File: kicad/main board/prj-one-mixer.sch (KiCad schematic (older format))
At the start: 51 parts, among them U301 TL072, U302 TL072, U303 TL072

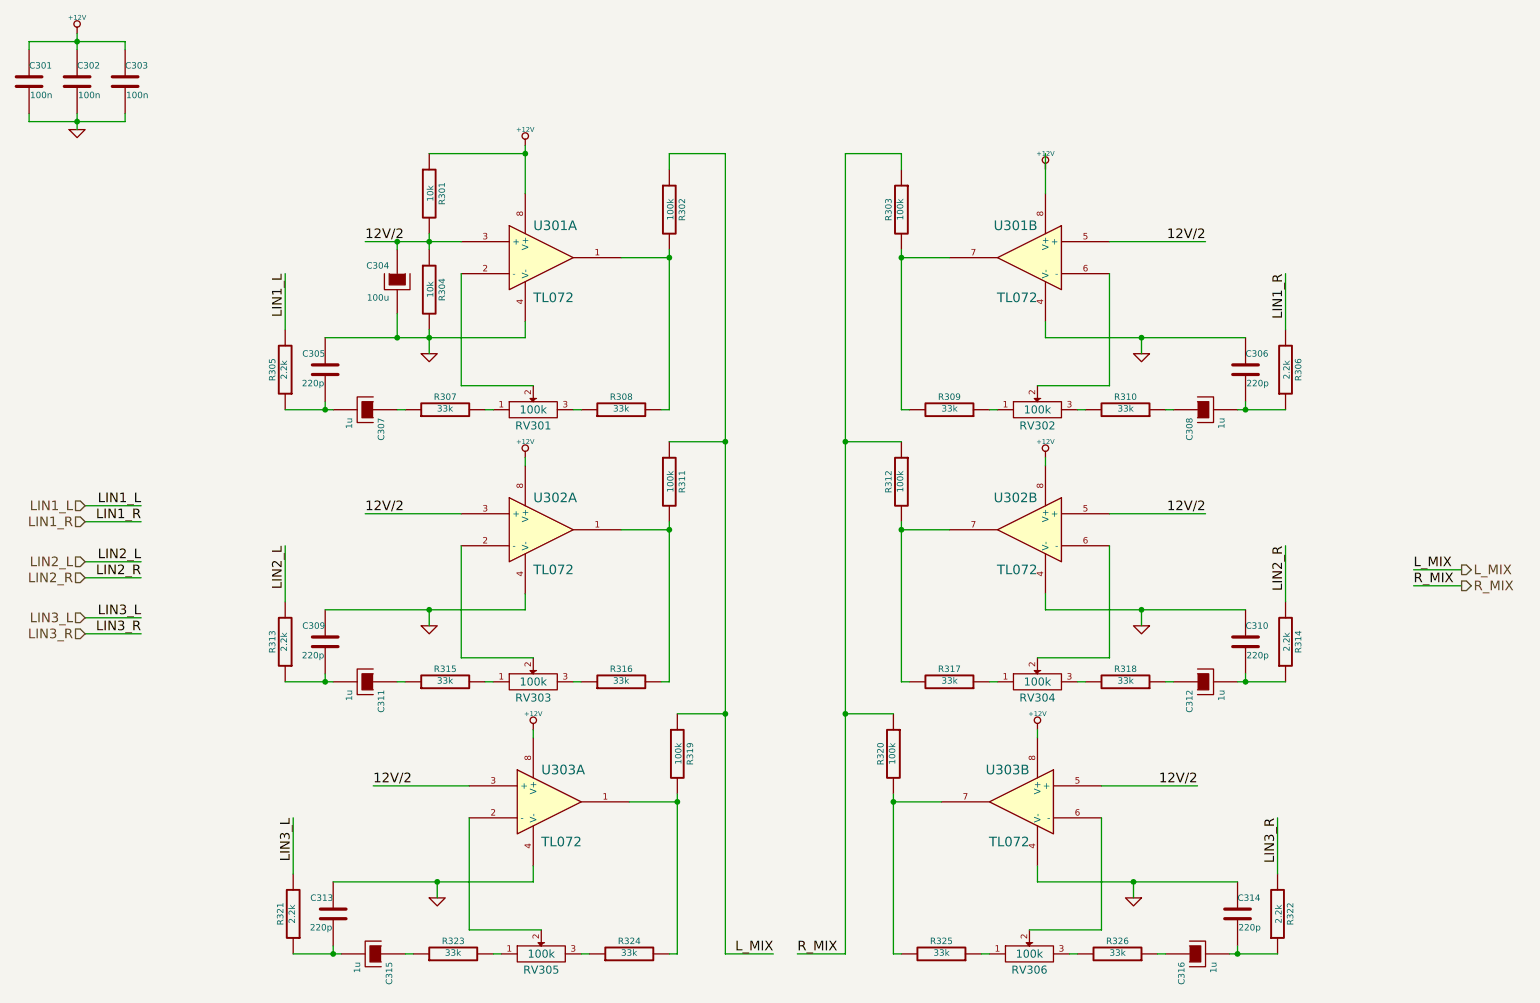
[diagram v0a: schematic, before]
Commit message: Simplify mixer design, remove power amp
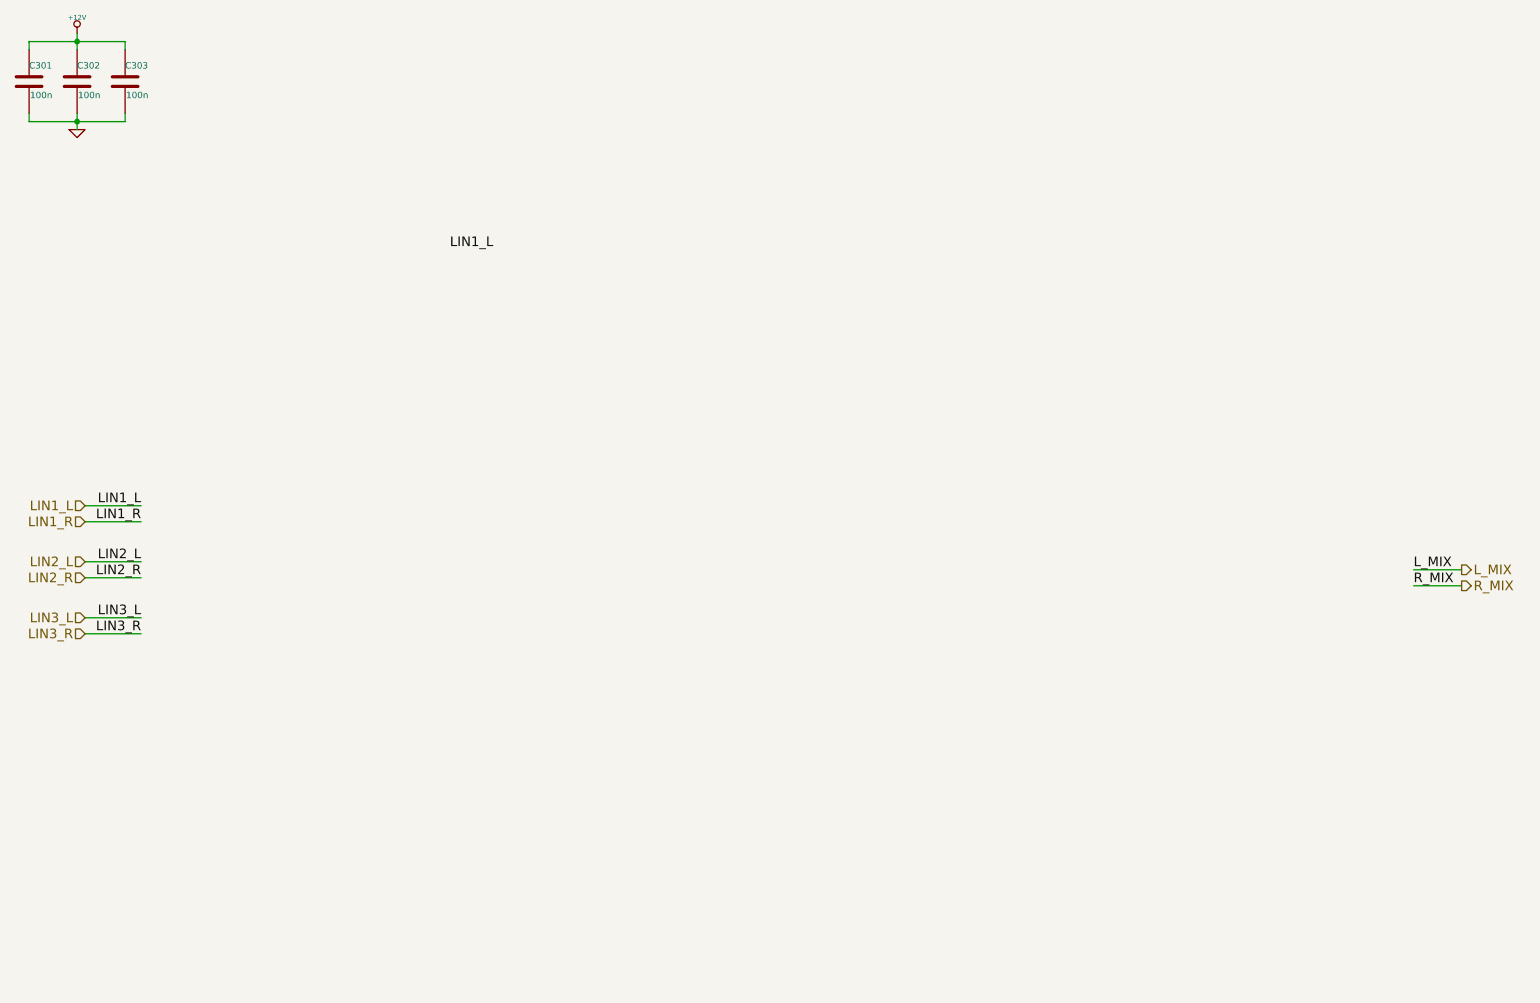
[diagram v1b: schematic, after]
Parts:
- removed C304: 100u, ~, symbol CAPAPOL
- removed C305, C306, C309, C310, C313, C314: 220p, ~, symbol C
- removed C307, C308, C311, C312, C315, C316: 1u, ~, symbol CAPAPOL
- removed R301, R304: 10k, ~, symbol R
- removed R302, R303, R311, R312, R319, R320: 100k, ~, symbol R
- removed R305, R306, R313, R314, R321, R322: 2.2k, ~, symbol R
- removed R307, R308, R309, R310, R315, R316, R317, R318, R323, R324, R325, R326: 33k, ~, symbol R
- removed RV301, RV302, RV303, RV304, RV305, RV306: 100k, ~, symbol POT
- removed U301, U302, U303: TL072, symbol TL072
